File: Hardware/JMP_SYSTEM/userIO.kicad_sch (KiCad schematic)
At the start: 26 parts

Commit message: Schematics and PCB layout
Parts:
- removed R? (x5): 500, Resistor_SMD:R_0805_2012Metric_Pad1.20x1.40mm_HandSolder, symbol Device:R
- added C10, C8, C9: 0.1uF, Resistor_SMD:R_0805_2012Metric_Pad1.20x1.40mm_HandSolder, symbol Device:C_Small
- added J12: RELE, Connector_PinHeader_2.54mm:PinHeader_1x03_P2.54mm_Vertical, symbol Connector_Generic:Conn_01x03
- added J22, J9: Debug, Connector_PinHeader_2.54mm:PinHeader_1x02_P2.54mm_Vertical, symbol Connector_Generic:Conn_01x02
- added R15, R17, R19: 100K, Resistor_SMD:R_0805_2012Metric_Pad1.20x1.40mm_HandSolder, symbol Device:R
- added R16, R18, R20: 10K, Resistor_SMD:R_0805_2012Metric_Pad1.20x1.40mm_HandSolder, symbol Device:R
- added SW10: BT_RST, Connector_Molex:Molex_KK-254_AE-6410-02A_1x02_P2.54mm_Vertical, symbol Switch:SW_DIP_x01
- added SW8: BT_MENU, Connector_Molex:Molex_KK-254_AE-6410-02A_1x02_P2.54mm_Vertical, symbol Switch:SW_DIP_x01
- added SW9: BT_OK, Connector_Molex:Molex_KK-254_AE-6410-02A_1x02_P2.54mm_Vertical, symbol Switch:SW_DIP_x01
- added U1: LCD-PCF8574, adelson:Módulo I2C - PCF8574, symbol adelson:LCD-PCF8574
- SW3: renamed from SW?; value BT_AVANCAR -> BT_LEFT
- SW4: renamed from SW?; value BT_SELECT -> BT_RIGHT
- SW5: renamed from SW?; value BT_MENU -> BT_UP
- SW6: renamed from SW?; value BT_INSERT -> BT_DOWN
- U2: renamed from U?; footprint Display:LCD-016N002L -> Connector_PinHeader_2.54mm:PinHeader_1x16_P2.54mm_Vertical
- gave numbers to parts that had none: 16
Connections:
- net 3V3: now also R15.1, R17.1, R19.1
- net 5V: now also J22.1 (Pin_1), J9.1 (Pin_1); no longer U2.2 (VDD)
- net BT_MENU: now also C8.1, R16.2; no longer C5.1, R10.2
- net E: now also U1.6 (E)
- net GNDD: now also C10.2, C8.2, C9.2, J12.2 (Pin_2), SW10.1, SW8.1, SW9.1, U1.1 (VSS_DISP), U1.20 (VSS)
- net RS: now also U1.4 (RS)
- net R/~{W}: now also U1.5 (R/~{W})
- net A renamed LED_AN
- net LED_AN: now also U1.15 (A)
- net BT_AVANCAR renamed BT_LEFT
- net BT_INSERT renamed BT_DOWN
- net BT_SELECT renamed BT_RIGHT
- net DB0: no longer names the net of U2.7 (DB0)
- net DB0: now also U1.7 (DB0)
- net DB1: no longer names the net of U2.8 (DB1)
- net DB1: now also U1.8 (DB1)
- net DB2: no longer names the net of U2.9 (DB2)
- net DB2: now also U1.9 (DB2)
- net DB3: no longer names the net of U2.10 (DB3)
- net DB3: now also U1.10 (DB3)
- net DB4: no longer names the net of U2.11 (DB4)
- net DB4: now also U1.11 (DB4)
- net DB5: no longer names the net of U2.12 (DB5)
- net DB5: now also U1.12 (DB5)
- net DB6: no longer names the net of U2.13 (DB6)
- net DB6: now also U1.13 (DB6)
- net DB7: no longer names the net of U2.14 (DB7)
- net DB7: now also U1.14 (DB7)
- net K renamed LED_CAT
- net LED_CAT: now also U1.16 (K)
- net V0 renamed VO
- net VO: now also U1.3 (VO)
- new net: R19.2, R20.1, SW10.2
- new net: R17.2, R18.1, SW9.2
- new net: R15.2, R16.1, SW8.2
- new net: J12.1 (Pin_1), J22.2 (Pin_2)
- new net: J9.2 (Pin_2), U1.19 (VDD)
- new net BT_OK: C9.1, R18.2
- new net BT_RST: C10.1, R20.2
- new net BT_UP: C5.1, R10.2
- new net RELE: J12.3 (Pin_3)
- new net SCL: U1.17 (SCL)
- new net SDA: U1.18 (SDA)
- new net VDD_DISP: U1.2 (VDD_DISP), U2.2 (VDD)
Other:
- note added: "I2C/LCD PCF8574 Dimensões: 42 x 20 x 15mm https://curtocircuito.com.br/modulo-serial-i2c-p-display-lcd-pcf8574.html"
- note removed: "25mA max/pin"
- moved on the sheet: C3, C4, C5, C6, C7, R10, R11, R12, R13, R14, R5, R6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

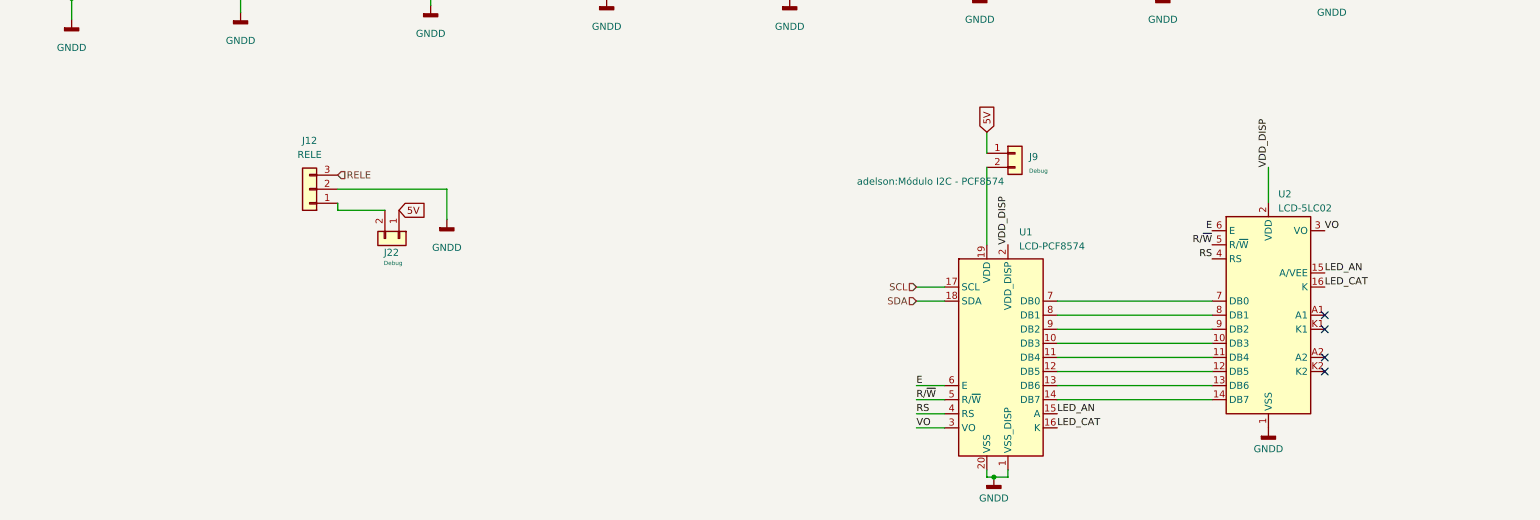
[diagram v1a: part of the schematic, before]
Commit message: Roteamento considerando I2C e Display em conjunto. O display ficara suspenso. Adicionado molex em todos os conectores. Debugs sao pinos convencionais
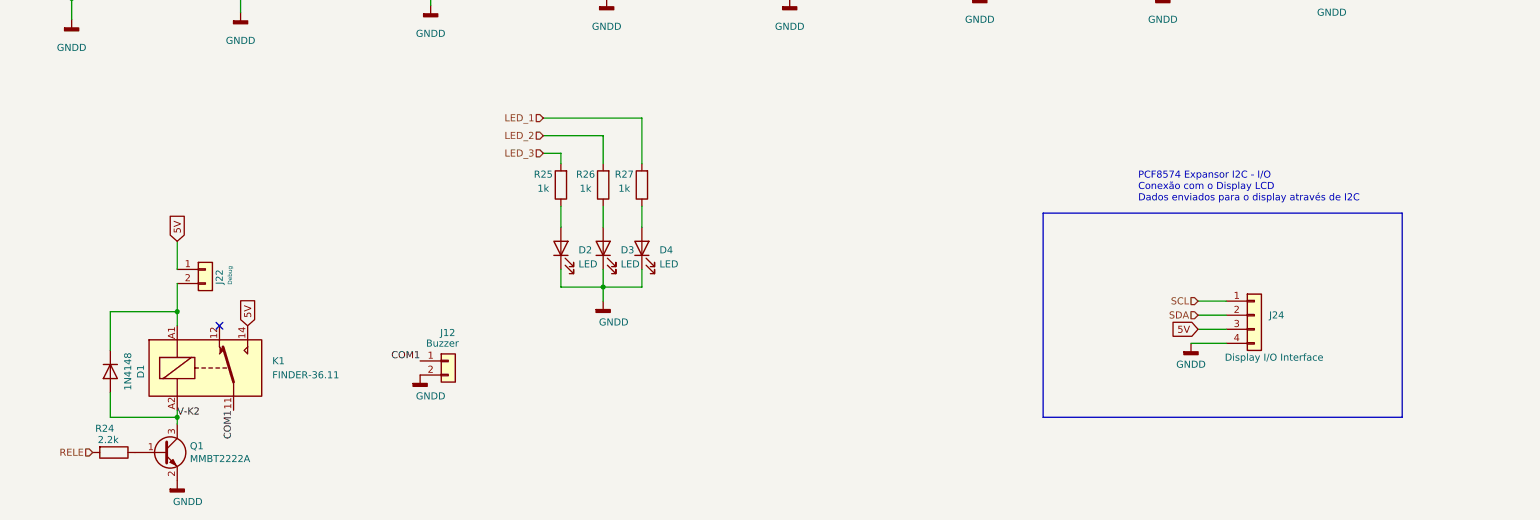
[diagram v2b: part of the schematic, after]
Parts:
- removed J12: RELE, Connector_PinHeader_2.54mm:PinHeader_1x03_P2.54mm_Vertical, symbol Connector_Generic:Conn_01x03
- removed J9: Debug, Connector_PinHeader_2.54mm:PinHeader_1x02_P2.54mm_Vertical, symbol Connector_Generic:Conn_01x02
- removed U1: LCD-PCF8574, adelson:Módulo I2C - PCF8574, symbol adelson:LCD-PCF8574
- removed U2: LCD-5LC02, Connector_PinHeader_2.54mm:PinHeader_1x16_P2.54mm_Vertical, symbol Display_Character:LCD-016N002L
- added D1: 1N4148, Diode_SMD:D_MiniMELF_Handsoldering, symbol Diode:1N4148
- added D2, D3, D4: LED, Connector_Molex:Molex_KK-254_AE-6410-02A_1x02_P2.54mm_Vertical, symbol Device:LED
- added J12: Buzzer, Connector_Molex:Molex_KK-254_AE-6410-02A_1x02_P2.54mm_Vertical, symbol Connector_Generic:Conn_01x02
- added J24: Display I/O Interface, Connector_Molex:Molex_KK-254_AE-6410-04A_1x04_P2.54mm_Vertical, symbol Connector_Generic:Conn_01x04
- added K1: FINDER-36.11, Relay_THT:Relay_SPDT_Finder_36.11, symbol Relay:FINDER-36.11
- added Q1: MMBT2222A, Package_TO_SOT_SMD:SOT-23, symbol Device:Q_NPN_BEC
- added R24: 2.2k, Resistor_SMD:R_1206_3216Metric_Pad1.30x1.75mm_HandSolder, symbol Device:R
- added R25, R26, R27: 1k, Resistor_SMD:R_0805_2012Metric_Pad1.20x1.40mm_HandSolder, symbol Device:R
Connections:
- net 5V: now also J24.3 (Pin_3), K1.14
- net GNDD: now also D2.1 (K), D3.1 (K), D4.1 (K), J12.2 (Pin_2), J24.4 (Pin_4), Q1.2 (E)
- net RELE: now also R24.2
- net SCL: now also J24.1 (Pin_1)
- net SDA: now also J24.2 (Pin_2)
- net at J22.2 (Pin_2): now also D1.1 (K), K1.A1
- new net: D4.2 (A), R27.1
- new net: D3.2 (A), R26.1
- new net: Q1.1 (B), R24.1
- new net: D2.2 (A), R25.1
- new net COM1: J12.1 (Pin_1), K1.11
- new net LED_1: R27.2
- new net LED_2: R26.2
- new net LED_3: R25.2
- new net V-K2: D1.2 (A), K1.A2, Q1.3 (C)
- no-connect marks 4 -> 1
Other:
- note added: "PCF8574 Expansor I2C - I/O Conexão com o Display LCD Dados enviados para o display através de I2C"
- moved on the sheet: J22
